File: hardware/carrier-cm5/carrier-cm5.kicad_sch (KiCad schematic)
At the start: 0 parts

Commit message: Added more ICs for power board
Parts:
- added C201: 100n, Capacitor_SMD:C_0603_1608Metric, symbol Device:C
- added C213: 100n, Capacitor_SMD:C_0805_2012Metric, symbol Device:C
- added C214, C218, C219: 15u, Capacitor_SMD:C_0805_2012Metric, symbol Device:C
- added C215: 1u, Capacitor_SMD:C_0805_2012Metric, symbol Device:C
- added C216: 22n, Capacitor_SMD:C_0805_2012Metric, symbol Device:C
- added C217: 100p, Capacitor_SMD:C_0805_2012Metric, symbol Device:C
- added IC203: TPS56A37RPAR, side-board:TPS56A37RPAR, symbol side-board:TPS56A37RPAR
- added L201: 3.3u, symbol Device:L
- added R201: 10k, Resistor_SMD:R_0603_1608Metric, symbol Device:R
- added R217, R218: 100k, Resistor_SMD:R_0603_1608Metric, symbol Device:R
- added R230: 52.3k, Resistor_SMD:R_0603_1608Metric, symbol Device:R
- added R231: 73.2k, Resistor_SMD:R_0805_2012Metric, symbol Device:R
- added R232: 10k, Resistor_SMD:R_0805_2012Metric, symbol Device:R
- added RT201: NCP18XH103F03RB, vector:THRMC1608X95N, symbol vector:NCP18XH103F03RB
- added TP213: BUCK_EN, TestPoint:TestPoint_Pad_D2.0mm, symbol Connector:TestPoint
- added TP214: BUCK_PG, TestPoint:TestPoint_Pad_D2.0mm, symbol Connector:TestPoint
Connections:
- new net: C213.1, IC203.7 (BOOT)
- new net: C213.2, IC203.6 (SW), L201.2
- new net +3V3: R201.1, R218.2
- new net 6V0_BUCK: C217.2, C218.2, C219.2, L201.1, R231.1
- new net BUCK_EN: IC203.1 (EN), R217.2, TP213.1
- new net BUCK_FB: C217.1, IC203.2 (FB), R231.2, R232.1
- new net BUCK_MODE: IC203.10 (MODE), R230.2
- new net BUCK_PG: IC203.4 (PG), R218.1, TP214.1
- new net BUCK_SS: C216.1, IC203.5 (SS)
- new net GND: C201.2, C214.2, C215.2, C216.2, C218.1, C219.1, IC203.3 (AGND), IC203.9 (PGND), R217.1, R230.1, R232.2, RT201.2
- new net NTC_SENSE: C201.1, R201.2, RT201.1
- new net VBAT: C214.1, C215.1, IC203.11 (VIN_2), IC203.12 (VIN_3), IC203.13 (VIN_4), IC203.8 (VIN_1)
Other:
- note added: "5V Buck Step-Down Converter"
- note added: "NTC Sensor"

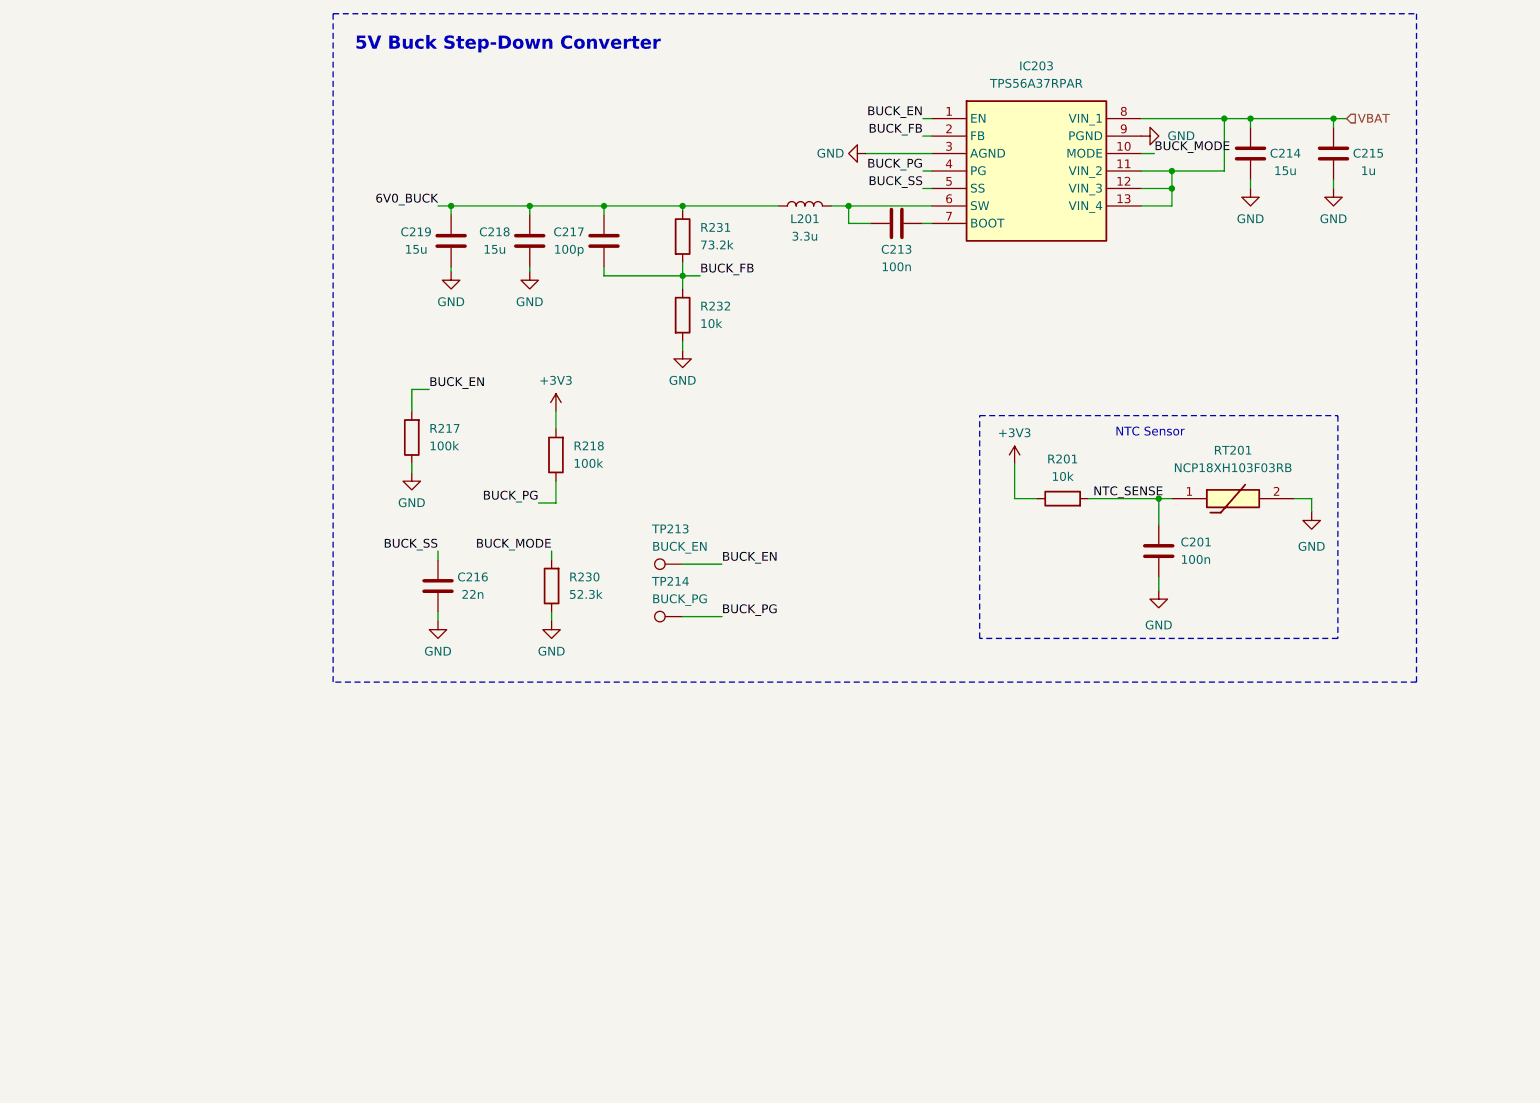
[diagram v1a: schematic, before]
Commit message: cm5 carrier: base on the cm5 io board, usb3, m.2, two csi, fan, test points
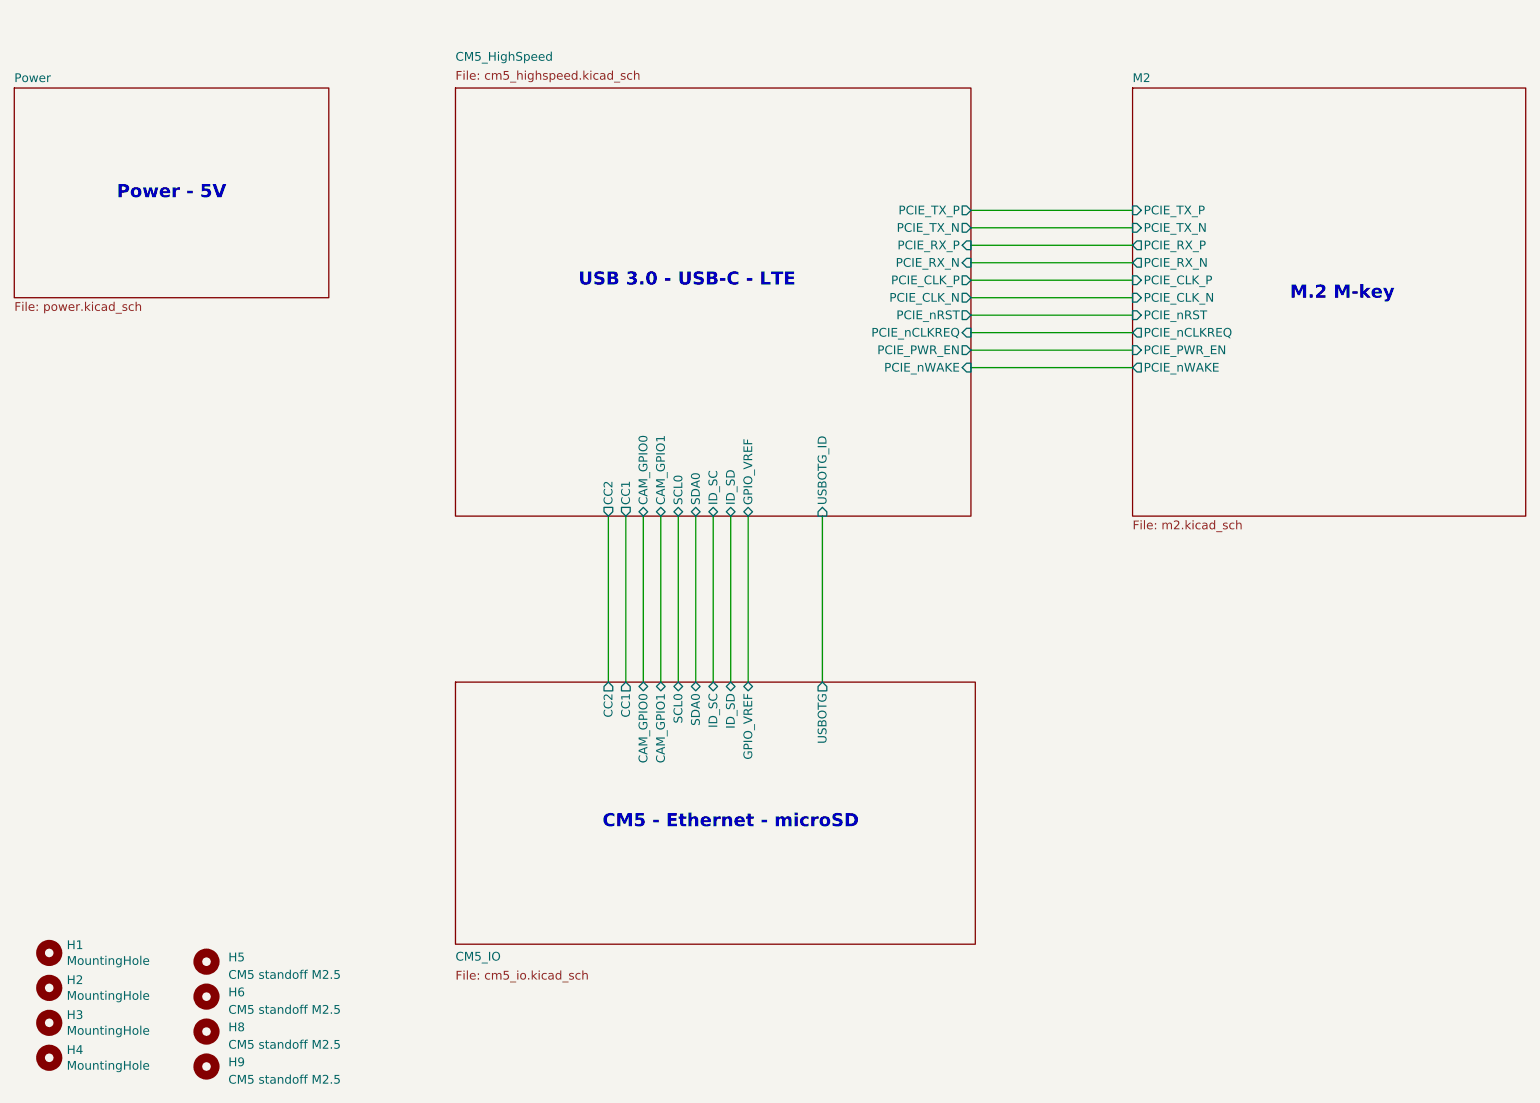
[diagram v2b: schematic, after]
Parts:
- removed C201: 100n, Capacitor_SMD:C_0603_1608Metric, symbol Device:C
- removed C213: 100n, Capacitor_SMD:C_0805_2012Metric, symbol Device:C
- removed C214, C218, C219: 15u, Capacitor_SMD:C_0805_2012Metric, symbol Device:C
- removed C215: 1u, Capacitor_SMD:C_0805_2012Metric, symbol Device:C
- removed C216: 22n, Capacitor_SMD:C_0805_2012Metric, symbol Device:C
- removed C217: 100p, Capacitor_SMD:C_0805_2012Metric, symbol Device:C
- removed IC203: TPS56A37RPAR, side-board:TPS56A37RPAR, symbol side-board:TPS56A37RPAR
- removed L201: 3.3u, symbol Device:L
- removed R201: 10k, Resistor_SMD:R_0603_1608Metric, symbol Device:R
- removed R217, R218: 100k, Resistor_SMD:R_0603_1608Metric, symbol Device:R
- removed R230: 52.3k, Resistor_SMD:R_0603_1608Metric, symbol Device:R
- removed R231: 73.2k, Resistor_SMD:R_0805_2012Metric, symbol Device:R
- removed R232: 10k, Resistor_SMD:R_0805_2012Metric, symbol Device:R
- removed RT201: NCP18XH103F03RB, vector:THRMC1608X95N, symbol vector:NCP18XH103F03RB
- removed TP213: BUCK_EN, TestPoint:TestPoint_Pad_D2.0mm, symbol Connector:TestPoint
- removed TP214: BUCK_PG, TestPoint:TestPoint_Pad_D2.0mm, symbol Connector:TestPoint
- added H1, H2, H3, H4: MountingHole, MountingHole:MountingHole_3.2mm_M3_DIN965_Pad, symbol Mechanical:MountingHole
- added H5, H6, H8, H9: CM5 standoff M2.5, vector:MountingHole_2.7mm_M2.5_DIN965, symbol Mechanical:MountingHole
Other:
- added sheet CM5_HighSpeed (cm5_highspeed.kicad_sch)
- added sheet CM5_IO (cm5_io.kicad_sch)
- added sheet M2 (m2.kicad_sch)
- added sheet Power (power.kicad_sch)
- note added: "CM5 - Ethernet - microSD"
- note added: "M.2 M-key"
- note added: "Power - 5V"
- note added: "USB 3.0 - USB-C - LTE"
- note removed: "5V Buck Step-Down Converter"
- note removed: "NTC Sensor"
- company: (none) -> AAC
- title: (none) -> V.E.C.T.O.R. - CM5 Carrier

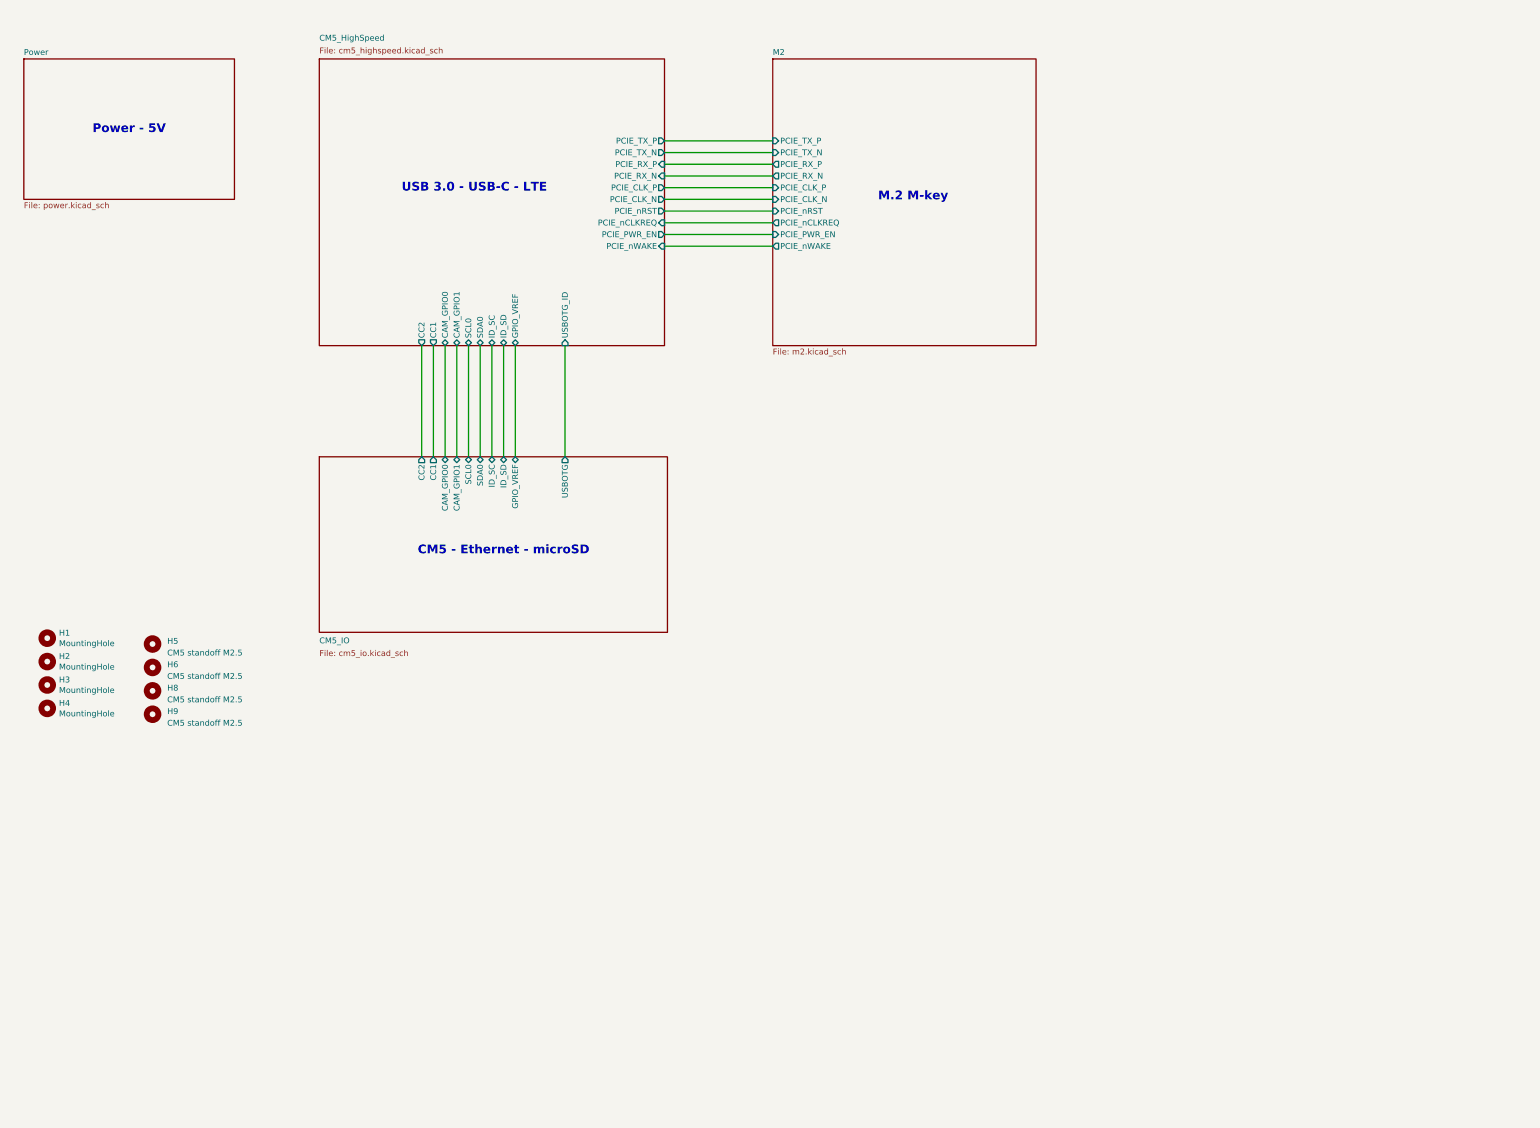
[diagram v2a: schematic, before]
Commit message: cm5 carrier: io mcu sheet (elrs, lidar, lora, adc, buzzer) and gnss sheet
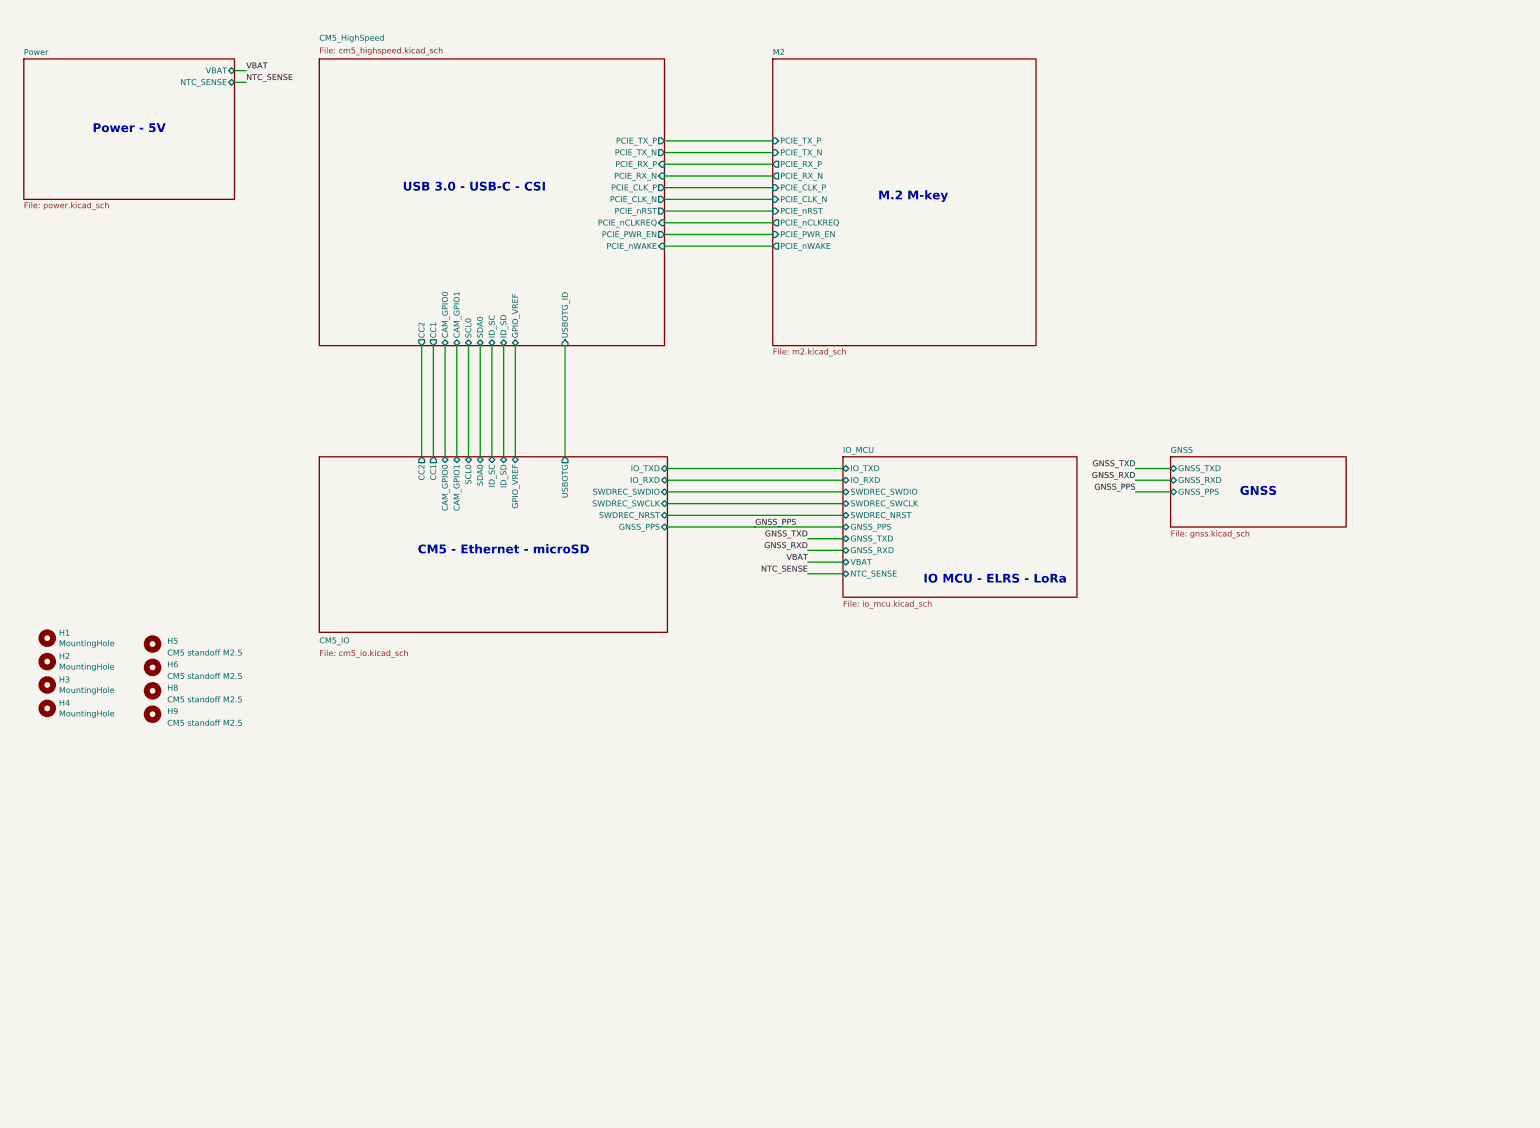
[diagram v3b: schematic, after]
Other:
- added sheet GNSS (gnss.kicad_sch)
- added sheet IO_MCU (io_mcu.kicad_sch)
- sheet CM5_IO ports: added GNSS_PPS, IO_RXD, IO_TXD, SWDREC_NRST, SWDREC_SWCLK, SWDREC_SWDIO; removed none
- sheet Power ports: added NTC_SENSE, VBAT; removed none
- note added: "GNSS"
- note added: "IO MCU - ELRS - LoRa"
- note added: "USB 3.0 - USB-C - CSI"
- note removed: "USB 3.0 - USB-C - LTE"

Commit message: cm5 carrier: a7670e lte sheet
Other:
- added sheet LTE (lte.kicad_sch)
- sheet CM5_IO ports: added LTE_PWRKEY, LTE_RXD, LTE_SLEEP, LTE_TXD; removed none
- sheet IO_MCU ports: added LTE_EN, LTE_STATUS; removed none
- note added: "LTE"

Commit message: cm5 carrier: can, imu, j-nose, swd recovery, j-sysctl gpios
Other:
- added sheet Peripherals (periph.kicad_sch)
- sheet CM5_IO ports: added CAN_CS, CAN_INT, CAN_MISO, CAN_MOSI, CAN_SCK, ESTOP_N, HALTED, I2C1_SCL, I2C1_SDA, IMU_INT, MAG_INT, SHUTDOWN_REQ_N, TOF_INT, TOF_LPN; removed none
- sheet Power ports: added ESTOP_N, HALTED, SHUTDOWN_REQ_N; removed none
- note added: "CAN - IMU - J-NOSE - SWD"
